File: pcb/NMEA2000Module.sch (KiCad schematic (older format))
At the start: 37 parts, among them IC1 MCP2562FD, IC2 MAX485/3485, K1 1W1, K2 1W2, K3 1W3, K4 1W4, P1 PULSE_IN, P10 I2C3, P2 RS-485 A/B, P3 CAN H/L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

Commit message: Adapted from SignalK to NMEA2000 device
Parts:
- removed K2: 1W2, Pin_Headers:Pin_Header_Straight_1x03_Pitch2.54mm, symbol CONN_3
- removed K3: 1W3, Pin_Headers:Pin_Header_Straight_1x03_Pitch2.54mm, symbol CONN_3
- removed K4: 1W4, Pin_Headers:Pin_Header_Straight_1x03_Pitch2.54mm, symbol CONN_3
- removed P10: I2C3, Pin_Headers:Pin_Header_Straight_1x04_Pitch2.54mm, symbol CONN_4
- removed P4, P5: CONN_1, Pin_Headers:Pin_Header_Straight_1x01_Pitch2.54mm, symbol CONN_1
- removed P6: ADS1115, Pin_Headers:Pin_Header_Straight_1x10_Pitch2.54mm, symbol CONN_10
- removed P8: I2C2, Pin_Headers:Pin_Header_Straight_1x04_Pitch2.54mm, symbol CONN_4
- added C5, C6, C7, C8: 10nF, Capacitors_SMD:C_0805_HandSoldering, symbol C
- added P4: CAN, Pin_Headers:Pin_Header_Straight_1x04_Pitch2.54mm, symbol CONN_4
- added R15, R16: 4K7, Resistors_SMD:R_0805_HandSoldering, symbol R
- added R17: 120R, Resistors_SMD:R_0805_HandSoldering, symbol R
- added U3: JDY40, Divers:JDY-40-TH, symbol JDY40
- added U4: DCDCConverter, Divers:DC-DC-Converter, symbol DCDCConverter
- added U5: BMP280, Divers:BMP280, symbol BMP280
- added U6: ADS1115, Divers:ADS1115, symbol ADS1115
- C1, C2, C3, C4: footprint Resistors_ThroughHole:Resistor_Horizontal_RM7mm -> Capacitors_SMD:C_0805_HandSoldering
- P3: value CAN H/L -> TERM_R
- R1, R12, R2, R3, R4, R5: footprint Resistors_ThroughHole:Resistor_Horizontal_RM7mm -> Resistors_SMD:R_0805_HandSoldering
- R10, R13, R6, R8: value 4K7 -> 10K; footprint Resistors_ThroughHole:Resistor_Horizontal_RM7mm -> Resistors_SMD:R_0805_HandSoldering
- R11, R14, R7, R9: value 4K7 -> 2K2; footprint Resistors_ThroughHole:Resistor_Horizontal_RM7mm -> Resistors_SMD:R_0805_HandSoldering
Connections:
- net labels added: 12v, 3v3, CANH, CANL, RFEN, SERIALEN, SERIALRX, SERIALTX
- net labels removed: +3,3V, +5V, RS485-RX, RS485-TX, RS485-TXEN
- wire segments 143 -> 180
- no-connect marks 18 -> 30
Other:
- moved on the sheet: D1, R10, R13, R6, R8

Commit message: Added RF code not tested, and high voltage protection diodes
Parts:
- added D2, D3, D4, D5: DIODE, Resistors_ThroughHole:Resistor_Horizontal_RM7mm, symbol DIODE
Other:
- moved on the sheet: C2, C4, P1, R1, R2, R3, R4, U1A, U1B

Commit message: Added BMP280 sensor and changed to LDO regulator
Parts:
- removed D1: DIODE, Resistors_ThroughHole:Resistor_Horizontal_RM7mm, symbol DIODE
- removed IC2: MAX485/3485, Housings_DIP:DIP-8_W7.62mm_LongPads, symbol MAX485/3485
- removed P2: RS-485 A/B, Pin_Headers:Pin_Header_Straight_1x02_Pitch2.54mm, symbol CONN_2
- removed R5: 120R, Resistors_SMD:R_0805_HandSoldering, symbol R
- removed U4: DCDCConverter, Divers:DC-DC-Converter, symbol DCDCConverter
- added C10: 100nF, Capacitors_SMD:C_0805_HandSoldering, symbol C
- added C9: 330nF, Capacitors_SMD:C_0805_HandSoldering, symbol C
- added U4: 7805, TO_SOT_Packages_THT:TO-220_Neutral123_Horizontal_LargePads, symbol 7805
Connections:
- wire segments 180 -> 166
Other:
- note removed: "RS-485\n"
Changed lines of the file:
@@
 Text GLabel 3450 5050 0    60   Input ~ 0
 5v
-$Comp
-L GND #PWR05
-U 1 1 5F00EA6F
-P 6050 1600
-F 0 "#PWR05" H 6050 1600 30  0001 C CNN
-F 1 "GND" H 6050 1530 30  0001 C CNN
-F 2 "" H 6050 1600 60  0001 C CNN
-F 3 "" H 6050 1600 60  0001 C CNN
-	1    6050 1600
-	1    0    0    -1
-$EndComp
 Text GLabel 6200 900  2    60   Output ~ 0
 5v
 $Comp
-L GND #PWR06
+L GND #PWR05
 U 1 1 5F012588
 P 4300 7250
-F 0 "#PWR06" H 4300 7250 30  0001 C CNN
+F 0 "#PWR05" H 4300 7250 30  0001 C CNN
 F 1 "GND" H 4300 7180 30  0001 C CNN
 F 2 "" H 4300 7250 60  0001 C CNN
@@
 $EndComp
 $Comp
-L GND #PWR07
+L GND #PWR06
 U 1 1 5F0142AC
 P 1300 7700
-F 0 "#PWR07" H 1300 7700 30  0001 C CNN
+F 0 "#PWR06" H 1300 7700 30  0001 C CNN
 F 1 "GND" H 1300 7630 30  0001 C CNN
 F 2 "" H 1300 7700 60  0001 C CNN
 F 3 "" H 1300 7700 60  0001 C CNN
 	1    1300 7700
-	1    0    0    -1
-$EndComp
-$Comp
-L DIODE D1
-U 1 1 5F0CBF72
-P 4000 900
-F 0 "D1" H 4000 1000 40  0000 C CNN
-F 1 "DIODE" H 4000 800 40  0000 C CNN
-F 2 "Resistors_ThroughHole:Resistor_Horizontal_RM7mm" H 4000 900 60  0001 C CNN
-F 3 "" H 4000 900 60  0000 C CNN
-	1    4000 900
 	1    0    0    -1
 $EndComp
@@
 5v
 $Comp
-L GND #PWR08
+L GND #PWR07
 U 1 1 5F3F9A1A
 P 1700 2500
-F 0 "#PWR08" H 1700 2500 30  0001 C CNN
+F 0 "#PWR07" H 1700 2500 30  0001 C CNN
 F 1 "GND" H 1700 2430 30  0001 C CNN
 F 2 "" H 1700 2500 60  0001 C CNN
@@
 $EndComp
 $Comp
-L GND #PWR09
+L GND #PWR08
 U 1 1 5F3FA56B
 P 2250 1650
-F 0 "#PWR09" H 2250 1650 30  0001 C CNN
+F 0 "#PWR08" H 2250 1650 30  0001 C CNN
 F 1 "GND" H 2250 1580 30  0001 C CNN
 F 2 "" H 2250 1650 60  0001 C CNN
@@
 $EndComp
 $Comp
-L GND #PWR010
+L GND #PWR09
 U 1 1 5F3FA959
 P 800 2650
-F 0 "#PWR010" H 800 2650 30  0001 C CNN
+F 0 "#PWR09" H 800 2650 30  0001 C CNN
 F 1 "GND" H 800 2580 30  0001 C CNN
 F 2 "" H 800 2650 60  0001 C CNN
@@
 CAN Trancever
 $Comp
-L GND #PWR011
+L GND #PWR010
 U 1 1 5F3FD6B3
 P 9850 6850
-F 0 "#PWR011" H 9850 6850 30  0001 C CNN
+F 0 "#PWR010" H 9850 6850 30  0001 C CNN
 F 1 "GND" H 9850 6780 30  0001 C CNN
 F 2 "" H 9850 6850 60  0001 C CNN
@@
 SDA
 $Comp
-L GND #PWR012
+L GND #PWR011
 U 1 1 5F3FE6D4
 P 6550 5750
-F 0 "#PWR012" H 6550 5750 30  0001 C CNN
+F 0 "#PWR011" H 6550 5750 30  0001 C CNN
 F 1 "GND" H 6550 5680 30  0001 C CNN
 F 2 "" H 6550 5750 60  0001 C CNN
@@
 	1    0    0    -1
 $EndComp
-Text Notes 1600 3900 0    60   ~ 0
-RS-485\n
 Text Notes 3750 6650 0    60   ~ 0
 Digital In
@@
 Text GLabel 7700 3350 2    60   Input ~ 0
 CAN-RX
-$Comp
-L MAX485/3485 IC2
-U 1 1 5F408A98
-P 1800 4750
-F 0 "IC2" H 1550 5050 40  0000 C CNN
-F 1 "MAX485/3485" H 2050 4450 40  0000 C CNN
-F 2 "Housings_DIP:DIP-8_W7.62mm_LongPads" H 1800 4750 35  0000 C CIN
-F 3 "" H 1800 4750 60  0000 C CNN
-	1    1800 4750
-	1    0    0    -1
-$EndComp
-$Comp
-L GND #PWR013
-U 1 1 5F408DB6
-P 1800 5250
-F 0 "#PWR013" H 1800 5250 30  0001 C CNN
-F 1 "GND" H 1800 5180 30  0001 C CNN
-F 2 "" H 1800 5250 60  0001 C CNN
-F 3 "" H 1800 5250 60  0001 C CNN
-	1    1800 5250
-	1    0    0    -1
-$EndComp
-$Comp
-L CONN_2 P2
-U 1 1 5F408E33
-P 2800 4750
-F 0 "P2" V 2750 4750 40  0000 C CNN
-F 1 "RS-485 A/B" V 2850 4750 40  0000 C CNN
-F 2 "Pin_Headers:Pin_Header_Straight_1x02_Pitch2.54mm" H 2800 4750 60  0001 C CNN
-F 3 "" H 2800 4750 60  0001 C CNN
-	1    2800 4750
-	1    0    0    -1
-$EndComp
-Text GLabel 1100 4550 0    60   Input ~ 0
-SERIALTX
-Text GLabel 1100 4700 0    60   Input ~ 0
-SERIALEN
-Text GLabel 1100 4950 0    60   Output ~ 0
-SERIALRX
-$Comp
-L R R5
-U 1 1 5F409C50
-P 2350 5250
-F 0 "R5" V 2430 5250 40  0000 C CNN
-F 1 "120R" V 2357 5251 40  0000 C CNN
-F 2 "Resistors_SMD:R_0805_HandSoldering" V 2280 5250 30  0001 C CNN
-F 3 "" H 2350 5250 30  0000 C CNN
-	1    2350 5250
-	1    0    0    -1
-$EndComp
 NoConn ~ 7400 2550
 NoConn ~ 7400 2750
@@
 Text GLabel 10150 1000 2    60   Input ~ 0
 3v3
-Text GLabel 2050 4200 2    60   Input ~ 0
-3v3
 Text GLabel 700  1950 0    60   Input ~ 0
 3v3
 Text GLabel 2650 3600 2    60   Input ~ 0
 3v3
-$Comp
-L DCDCConverter U4
-U 1 1 5FEC9BAE
-P 5100 1200
-F 0 "U4" H 5100 1200 60  0000 C CNN
-F 1 "DCDCConverter" H 5100 1200 60  0000 C CNN
-F 2 "Divers:DC-DC-Converter" H 5100 1200 60  0001 C CNN
-F 3 "" H 5100 1200 60  0001 C CNN
-	1    5100 1200
-	1    0    0    -1
-$EndComp
 $Comp
 L R R7
@@
 RFEN
 $Comp
-L GND #PWR014
+L GND #PWR013
 U 1 1 60188B7E
 P 3150 3150
-F 0 "#PWR014" H 3150 3150 30  0001 C CNN
+F 0 "#PWR013" H 3150 3150 30  0001 C CNN
 F 1 "GND" H 3150 3080 30  0001 C CNN
 F 2 "" H 3150 3150 60  0001 C CNN
@@
 12v
 $Comp
-L GND #PWR015
+L GND #PWR014
 U 1 1 601925D8
 P 10850 3850
-F 0 "#PWR015" H 10850 3850 30  0001 C CNN
+F 0 "#PWR014" H 10850 3850 30  0001 C CNN
 F 1 "GND" H 10850 3780 30  0001 C CNN
 F 2 "" H 10850 3850 60  0001 C CNN
@@
 12v
 $Comp
-L GND #PWR016
+L GND #PWR015
 U 1 1 6019290E
-P 3500 1600
-F 0 "#PWR016" H 3500 1600 30  0001 C CNN
-F 1 "GND" H 3500 1530 30  0001 C CNN
-F 2 "" H 3500 1600 60  0001 C CNN
-F 3 "" H 3500 1600 60  0001 C CNN
-	1    3500 1600
+P 5000 1600
+F 0 "#PWR015" H 5000 1600 30  0001 C CNN
+F 1 "GND" H 5000 1530 30  0001 C CNN
+F 2 "" H 5000 1600 60  0001 C CNN
+F 3 "" H 5000 1600 60  0001 C CNN
+	1    5000 1600
 	1    0    0    -1
 $EndComp
@@
 3v3
 $Comp
-L GND #PWR017
+L GND #PWR016
 U 1 1 60195D59
 P 9900 2950
-F 0 "#PWR017" H 9900 2950 30  0001 C CNN
+F 0 "#PWR016" H 9900 2950 30  0001 C CNN
 F 1 "GND" H 9900 2880 30  0001 C CNN
 F 2 "" H 9900 2950 60  0001 C CNN
@@
 $EndComp
 $Comp
-L GND #PWR018
+L GND #PWR017
 U 1 1 60375A8F
 P 3600 7700
-F 0 "#PWR018" H 3600 7700 30  0001 C CNN
+F 0 "#PWR017" H 3600 7700 30  0001 C CNN
 F 1 "GND" H 3600 7630 30  0001 C CNN
 F 2 "" H 3600 7700 60  0001 C CNN
@@
 	3550 4950 3700 4950
 Wire Wire Line
-	5800 1500 6050 1500
-Wire Wire Line
-	6050 1500 6050 1600
-Wire Wire Line
 	4300 6700 4300 6950
 Wire Wire Line
@@
 	7400 3950 7700 3950
 Wire Wire Line
-	1100 4950 1350 4950
-Wire Wire Line
-	1100 4700 1200 4700
-Wire Wire Line
-	1200 4650 1200 4800
-Wire Wire Line
-	1200 4800 1350 4800
-Wire Wire Line
-	1100 4550 1350 4550
-Wire Wire Line
-	1350 4650 1200 4650
-Connection ~ 1200 4700
-Wire Wire Line
-	2250 4850 2450 4850
-Wire Wire Line
-	2250 4650 2450 4650
-Wire Wire Line
-	1800 5150 1800 5250
-Wire Wire Line
-	2350 5000 2350 4850
-Connection ~ 2350 4850
-Wire Wire Line
-	2350 5500 2350 5650
-Wire Wire Line
-	2350 5650 2450 5650
-Wire Wire Line
-	2450 5650 2450 4650
-Wire Wire Line
 	7400 3550 7700 3550
 Wire Wire Line
@@
 	2500 3100 3150 3100
 Wire Wire Line
-	2050 4200 1800 4200
-Wire Wire Line
-	1800 4200 1800 4350
-Wire Wire Line
 	10150 1000 9900 1000
 Wire Wire Line
@@
 	2650 3600 2500 3600
 Wire Wire Line
-	3650 900  3800 900
-Wire Wire Line
-	3500 1500 4350 1500
-Wire Wire Line
-	4200 900  4350 900
-Wire Wire Line
-	5800 900  6200 900
+	3650 900  4600 900
+Wire Wire Line
+	5400 900  6200 900
 Wire Wire Line
 	9950 4750 9950 4800
@@
 Wire Wire Line
 	8750 3000 9100 3000
-Wire Wire Line
-	3500 1600 3500 1500
 Wire Wire Line
 	2300 2100 2300 1800
@@
 	4800 7050 4950 7050
 Wire Wire Line
-	3750 7600 3750 7650
-Wire Wire Line
-	3750 7650 3450 7650
+	3750 7650 3750 7600
+Wire Wire Line
+	3450 7650 3750 7650
 Wire Wire Line
 	3450 7650 3450 7600
@@
 Wire Wire Line
 	1300 6000 1300 6450
+$Comp
+L 7805 U4
+U 1 1 603DDC06
+P 5000 950
+F 0 "U4" H 5150 754 60  0000 C CNN
+F 1 "7805" H 5000 1150 60  0000 C CNN
+F 2 "TO_SOT_Packages_THT:TO-220_Neutral123_Horizontal_LargePads" H 5000 950 60  0001 C CNN
+F 3 "" H 5000 950 60  0000 C CNN
+	1    5000 950
+	1    0    0    -1
+$EndComp
+$Comp
+L C C9
+U 1 1 603DE009
+P 4400 1200
+F 0 "C9" H 4400 1300 40  0000 L CNN
+F 1 "330nF" H 4406 1115 40  0000 L CNN
+F 2 "Capacitors_SMD:C_0805_HandSoldering" H 4438 1050 30  0001 C CNN
+F 3 "" H 4400 1200 60  0000 C CNN
+	1    4400 1200
+	1    0    0    -1
+$EndComp
+$Comp
+L C C10
+U 1 1 603DE0BF
+P 5600 1200
+F 0 "C10" H 5600 1300 40  0000 L CNN
+F 1 "100nF" H 5606 1115 40  0000 L CNN
+F 2 "Capacitors_SMD:C_0805_HandSoldering" H 5638 1050 30  0001 C CNN
+F 3 "" H 5600 1200 60  0000 C CNN
+	1    5600 1200
+	1    0    0    -1
+$EndComp
+Wire Wire Line
+	4400 1400 4400 1500
+Wire Wire Line
+	4400 1500 5600 1500
+Wire Wire Line
+	5600 1500 5600 1400
+Wire Wire Line
+	5000 1200 5000 1600
+Connection ~ 5000 1500
+Wire Wire Line
+	4400 1000 4400 900
+Connection ~ 4400 900
+Wire Wire Line
+	5600 1000 5600 900
+Connection ~ 5600 900
 $EndSCHEMATC

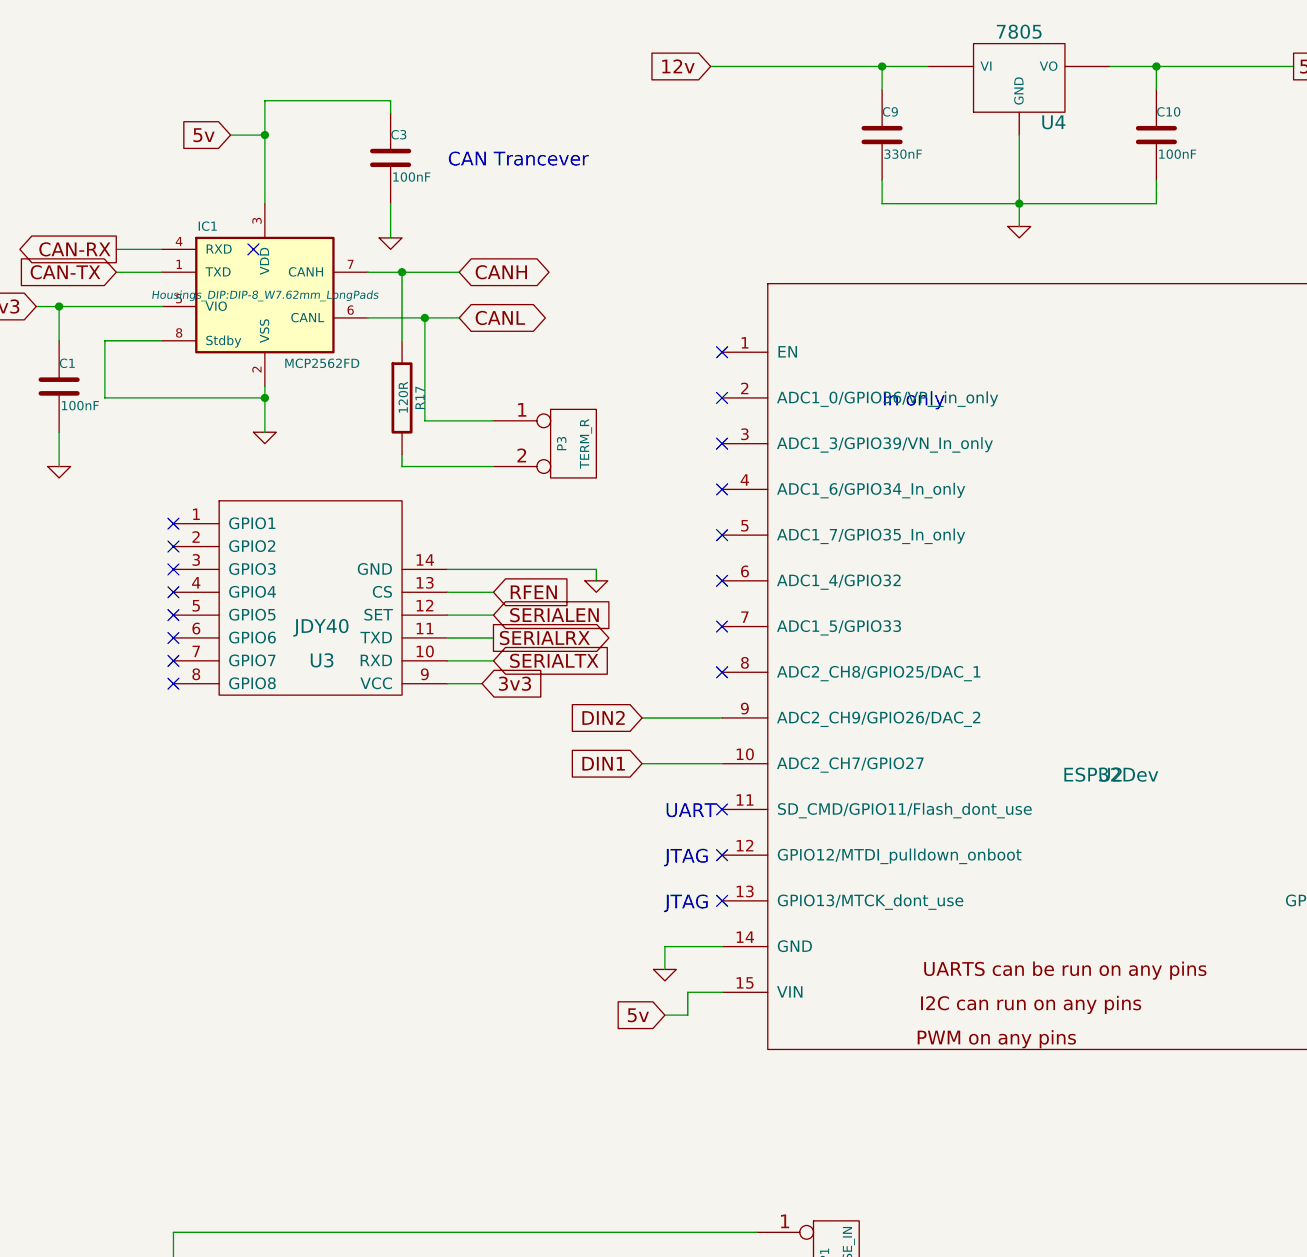
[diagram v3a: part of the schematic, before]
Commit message: Added BT switch and engine on support
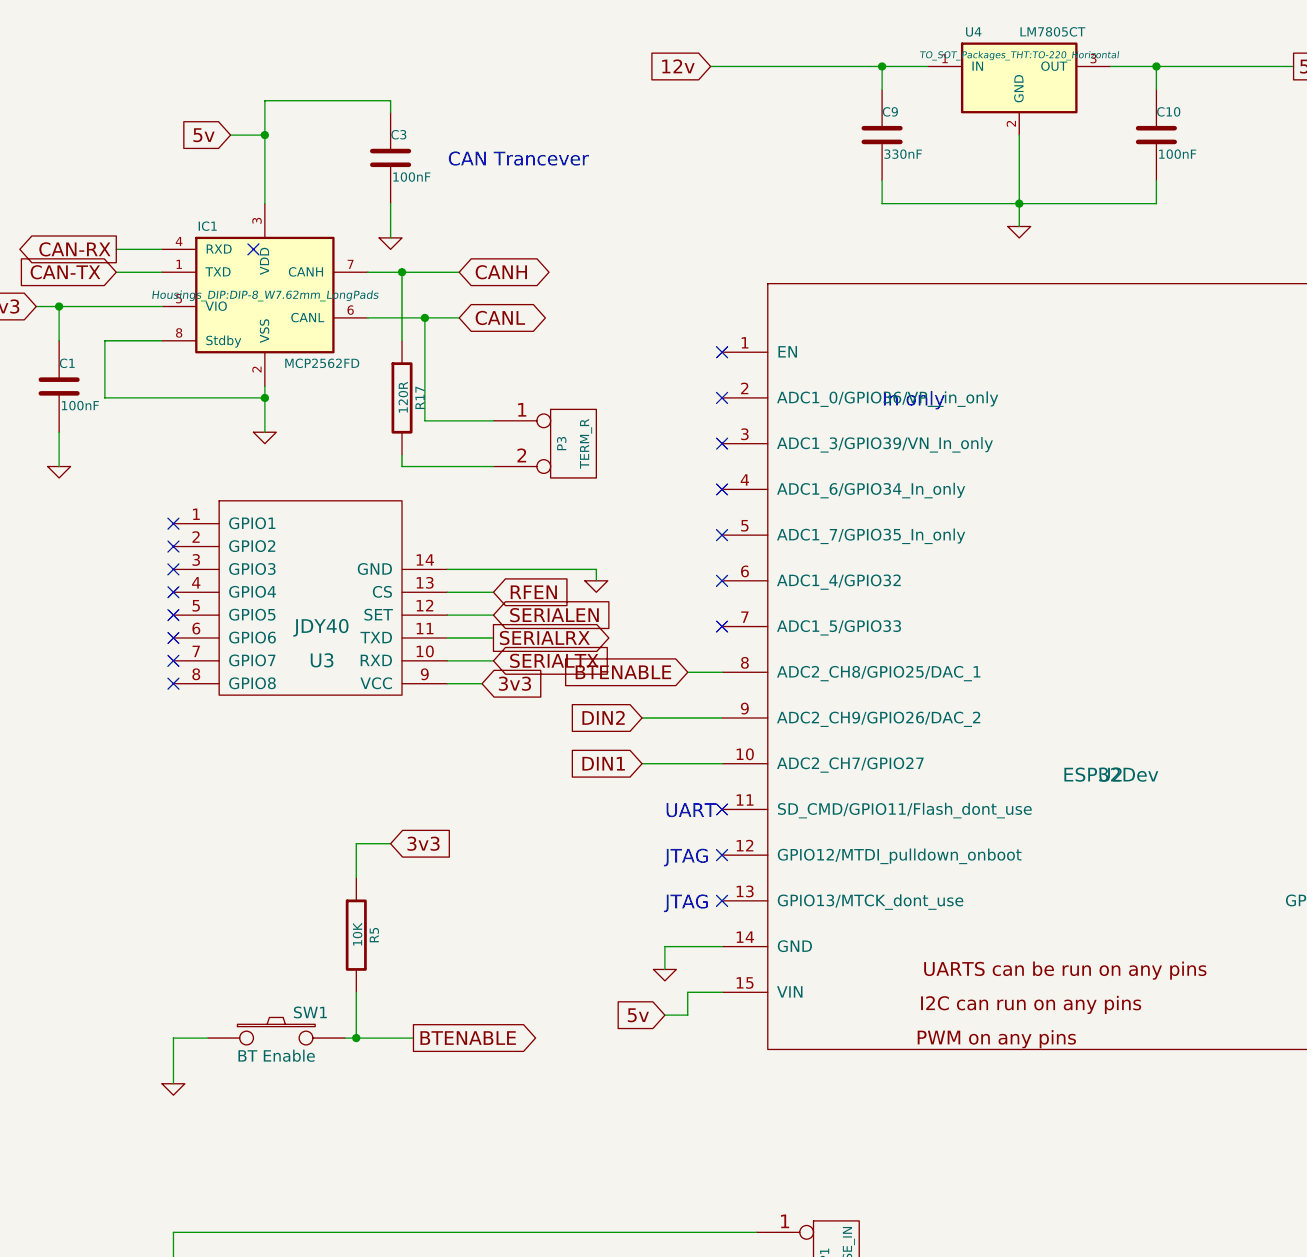
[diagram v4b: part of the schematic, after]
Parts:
- removed U4: 7805, TO_SOT_Packages_THT:TO-220_Neutral123_Horizontal_LargePads, symbol 7805
- added R5: 10K, Resistors_SMD:R_0805_HandSoldering, symbol R
- added SW1: BT Enable, Buttons_Switches_ThroughHole:SW_PUSH_6mm, symbol SW_PUSH
- added U4: LM7805CT, TO_SOT_Packages_THT:TO-220_Horizontal, symbol LM7805CT
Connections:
- net 12v: now also U4.1 (IN)
- net 3v3: now also R5.1
- net 5v: now also U4.3 (OUT)
- net GND: now also SW1.1, U4.2 (GND)
- net BTENABLE: now reaches U2.8 (ADC2_CH8/GPIO25/DAC_1)
- net BTENABLE: now also R5.2, SW1.2
- no-connect marks 30 -> 29
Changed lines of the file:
@@
 NoConn ~ 7400 4550
 NoConn ~ 7400 4350
-NoConn ~ 3700 3550
 NoConn ~ 3700 3350
 NoConn ~ 3700 3150
@@
 RFEN
 $Comp
-L GND #PWR013
+L GND #PWR012
 U 1 1 60188B7E
 P 3150 3150
-F 0 "#PWR013" H 3150 3150 30  0001 C CNN
+F 0 "#PWR012" H 3150 3150 30  0001 C CNN
 F 1 "GND" H 3150 3080 30  0001 C CNN
 F 2 "" H 3150 3150 60  0001 C CNN
@@
 12v
 $Comp
-L GND #PWR014
+L GND #PWR013
 U 1 1 601925D8
 P 10850 3850
-F 0 "#PWR014" H 10850 3850 30  0001 C CNN
+F 0 "#PWR013" H 10850 3850 30  0001 C CNN
 F 1 "GND" H 10850 3780 30  0001 C CNN
 F 2 "" H 10850 3850 60  0001 C CNN
@@
 12v
 $Comp
-L GND #PWR015
+L GND #PWR014
 U 1 1 6019290E
 P 5000 1600
-F 0 "#PWR015" H 5000 1600 30  0001 C CNN
+F 0 "#PWR014" H 5000 1600 30  0001 C CNN
 F 1 "GND" H 5000 1530 30  0001 C CNN
 F 2 "" H 5000 1600 60  0001 C CNN
@@
 3v3
 $Comp
-L GND #PWR016
+L GND #PWR015
 U 1 1 60195D59
 P 9900 2950
-F 0 "#PWR016" H 9900 2950 30  0001 C CNN
+F 0 "#PWR015" H 9900 2950 30  0001 C CNN
 F 1 "GND" H 9900 2880 30  0001 C CNN
 F 2 "" H 9900 2950 60  0001 C CNN
@@
 $EndComp
 $Comp
-L GND #PWR017
+L GND #PWR016
 U 1 1 60375A8F
 P 3600 7700
-F 0 "#PWR017" H 3600 7700 30  0001 C CNN
+F 0 "#PWR016" H 3600 7700 30  0001 C CNN
 F 1 "GND" H 3600 7630 30  0001 C CNN
 F 2 "" H 3600 7700 60  0001 C CNN
@@
 	1300 6000 1300 6450
 $Comp
-L 7805 U4
-U 1 1 603DDC06
-P 5000 950
-F 0 "U4" H 5150 754 60  0000 C CNN
-F 1 "7805" H 5000 1150 60  0000 C CNN
-F 2 "TO_SOT_Packages_THT:TO-220_Neutral123_Horizontal_LargePads" H 5000 950 60  0001 C CNN
-F 3 "" H 5000 950 60  0000 C CNN
-	1    5000 950
-	1    0    0    -1
-$EndComp
-$Comp
 L C C9
 U 1 1 603DE009
@@
 	5600 1000 5600 900
 Connection ~ 5600 900
+$Comp
+L LM7805CT U4
+U 1 1 603DFA56
+P 5000 950
+F 0 "U4" H 4800 1150 40  0000 C CNN
+F 1 "LM7805CT" H 5000 1150 40  0000 L CNN
+F 2 "TO_SOT_Packages_THT:TO-220_Horizontal" H 5000 1050 30  0000 C CIN
+F 3 "" H 5000 950 60  0000 C CNN
+	1    5000 950
+	1    0    0    -1
+$EndComp
+$Comp
+L SW_PUSH SW1
+U 1 1 6049C3C9
+P 1750 5150
+F 0 "SW1" H 1900 5260 50  0000 C CNN
+F 1 "BT Enable" H 1750 5070 50  0000 C CNN
+F 2 "Buttons_Switches_ThroughHole:SW_PUSH_6mm" H 1750 5150 60  0001 C CNN
+F 3 "" H 1750 5150 60  0000 C CNN
+	1    1750 5150
+	1    0    0    -1
+$EndComp
+$Comp
+L R R5
+U 1 1 6049C957
+P 2100 4700
+F 0 "R5" V 2180 4700 40  0000 C CNN
+F 1 "10K" V 2107 4701 40  0000 C CNN
+F 2 "Resistors_SMD:R_0805_HandSoldering" V 2030 4700 30  0001 C CNN
+F 3 "" H 2100 4700 30  0000 C CNN
+	1    2100 4700
+	1    0    0    -1
+$EndComp
+$Comp
+L GND #PWR017
+U 1 1 6049C9FC
+P 1300 5350
+F 0 "#PWR017" H 1300 5350 30  0001 C CNN
+F 1 "GND" H 1300 5280 30  0001 C CNN
+F 2 "" H 1300 5350 60  0001 C CNN
+F 3 "" H 1300 5350 60  0001 C CNN
+	1    1300 5350
+	1    0    0    -1
+$EndComp
+Wire Wire Line
+	1450 5150 1300 5150
+Wire Wire Line
+	1300 5150 1300 5350
+Wire Wire Line
+	2050 5150 2350 5150
+Wire Wire Line
+	2100 5150 2100 4950
+Text GLabel 2250 4300 2    60   Input ~ 0
+3v3
+Wire Wire Line
+	2100 4450 2100 4300
+Wire Wire Line
+	2100 4300 2250 4300
+Text GLabel 3550 3550 0    60   Input ~ 0
+BTENABLE
+Text GLabel 2350 5150 2    60   Output ~ 0
+BTENABLE
+Connection ~ 2100 5150
+Wire Wire Line
+	3550 3550 3700 3550
 $EndSCHEMATC
